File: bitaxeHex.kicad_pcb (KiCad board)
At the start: 4 copper layers, 84.5 x 129.5 mm, 358 parts, among them J1 Screw Terminal, J2 Conn_01x01, J3 Conn_02x05_Odd_Even, J4 TC2030-IDC, J5 Conn_01x04, J6 Conn_01x06, J7 USB_C_Receptacle_USB2.0, J8 Conn_01x04, J9 Conn_01x04, SW1 SWITCH-SPST, SW2 SWITCH-SPST, U1 LMR54410, U10 AP7331, U11 AP7331, U12 BM1366_mode1, U13 BM1366_mode1, U14 25MHz, U15 TLV3544, U16 AP7331, U17 AP7331, U18 BM1366_mode0, U19 25MHz, U2 RT9080-33GJ5, U20 BM1366_mode0, U21 TLV3544, U22 BM1366_mode1, U23 AP7331, U24 AP7331, U25 BM1366_mode1, U26 25MHz, U3 TPS546D24ARVFR, U4 MIC5504, U5 SN74AVC4T774, U6 ESP32-S3-WROOM-1, U7 TMP1075, U8 TMP1075, U9 EMC2302, Y1 32.768kHz

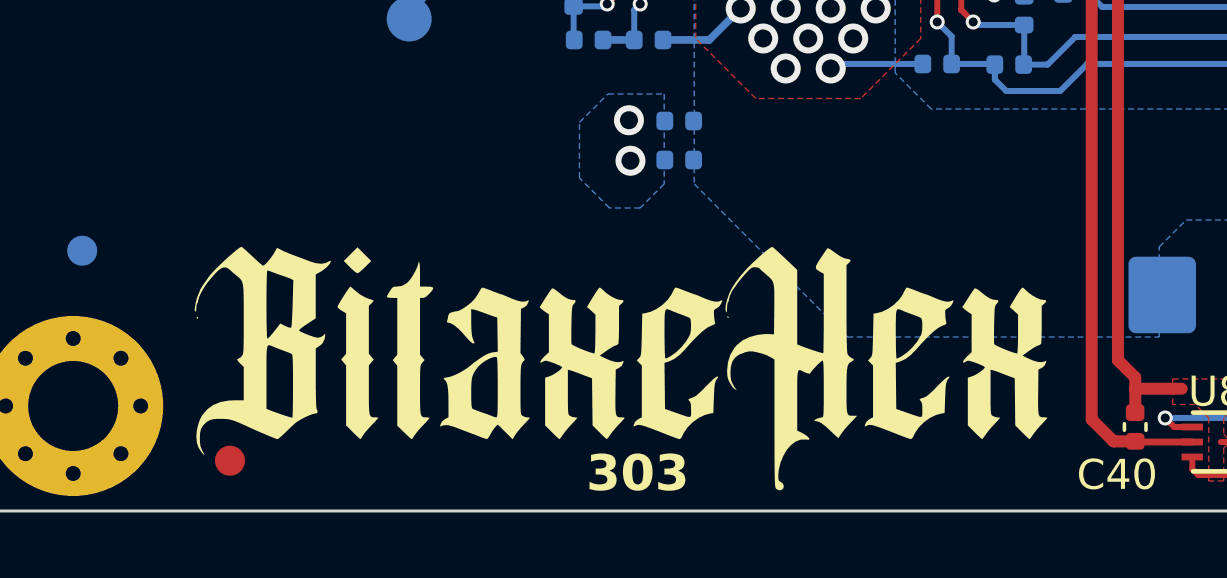
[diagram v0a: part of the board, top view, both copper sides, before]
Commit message: Move logo to F.Cu layer
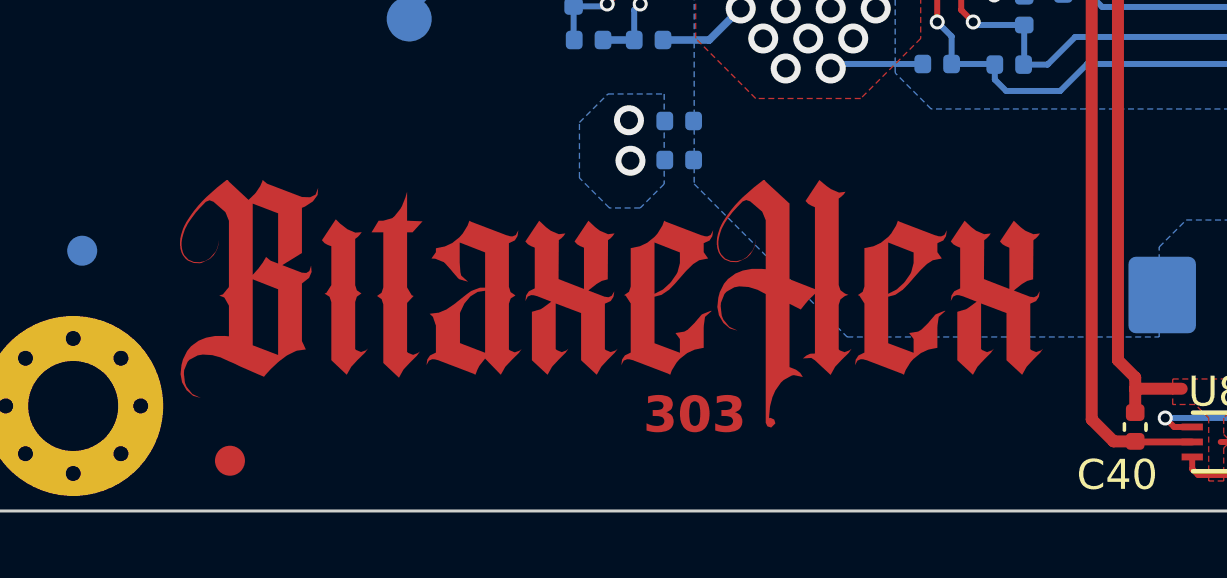
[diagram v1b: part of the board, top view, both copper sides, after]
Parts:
- moved G*** 2.80 mm to (71.5, 168.0)
